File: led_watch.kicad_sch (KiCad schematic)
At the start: 107 parts, among them U3 M0G3507QDGS32RQ1, Y2 TXC-7C

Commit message: 4 layers, removed regulator
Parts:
- removed C1, C2: 10uF, Capacitor_SMD:C_0805_2012Metric_Pad1.18x1.45mm_HandSolder, symbol Device:C
- removed C3: 0.1uF, Capacitor_SMD:C_0805_2012Metric_Pad1.18x1.45mm_HandSolder, symbol Device:C
- removed L1: 2.2uH, Inductor_SMD:L_0805_2012Metric_Pad1.15x1.40mm_HandSolder, symbol Device:L
- removed PS1: TPS63031DSKR, Package_SON:WSON-10-1EP_2.5x2.5mm_P0.5mm_EP1.2x2mm_ThermalVias, symbol TPS63031DSKR:TPS63031DSKR
- renumbered R14 to R10, R6 to R11, R15 to R12, R7 to R13, R16 to R14, R8 to R15, R17 to R16, R9 to R17, R10 to R2, R2 to R3, R11 to R4, R3 to R5, R12 to R6, R4 to R7, R13 to R8, R5 to R9
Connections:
- net +3V3 is gone; now on net +VBATT: C7.1, C8.1, R19.1, U3.7 (VDD), Y2.1 (EN), Y2.4 (Vdd)
- net PA10: now also R10.2
- net PA11/SPI0_SCK: no longer R11.1
- net PA12: now also R15.1, R16.2; no longer R13.1
- net PA13/TFT_D/C: now also R13.1, R14.2; no longer R15.1
- net PA16/SPI1_POCI: no longer R4.1
- net PA17/SPI1_CLK: no longer R6.1
- net PA18/SPI1_PICO/BSL_Invoke: no longer R8.1
- net PA2: now also R4.2
- net PA21: no longer R18.1
- net PA22: no longer R16.1
- net PA23: no longer R14.1
- net PA24/TFT_RESET: no longer R12.1
- net PA25/SPI1_CS3: now also R11.1, R12.2; no longer R10.1
- net PA4: now also R2.2
- net PA5/HFXIN: now also R6.2
- net PA7: now also R18.2
- net PA8/SPI0_CS0: now also R8.2
- net PA9: no longer R2.1
- net at D1.2 (A), D2.2 (A), D3.2 (A)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: now also R2.1; no longer R2.2
- net at D33.2 (A), D34.2 (A), D35.2 (A)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: now also R10.1; no longer R10.2
- net at D17.2 (A), D18.2 (A), D19.2 (A)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: now also R6.1; no longer R6.2
- net at D57.2 (A), D58.2 (A), D59.2 (A)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: now also R16.1; no longer R16.2
- net at D10.2 (A), D11.2 (A), D12.2 (A)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: now also R4.1; no longer R4.2
- net at D41.2 (A), D42.2 (A), D43.2 (A)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: now also R12.1; no longer R12.2
- net at D25.2 (A), D26.2 (A), D27.2 (A)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: now also R8.1; no longer R8.2
- net at D65.2 (A), D66.2 (A), D67.2 (A)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: now also R18.1; no longer R18.2
- net at D49.2 (A), D50.2 (A), D51.2 (A)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: now also R14.1; no longer R14.2
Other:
- moved on the sheet: R10, R12, R14, R16, R18, R2, R4, R6, R8

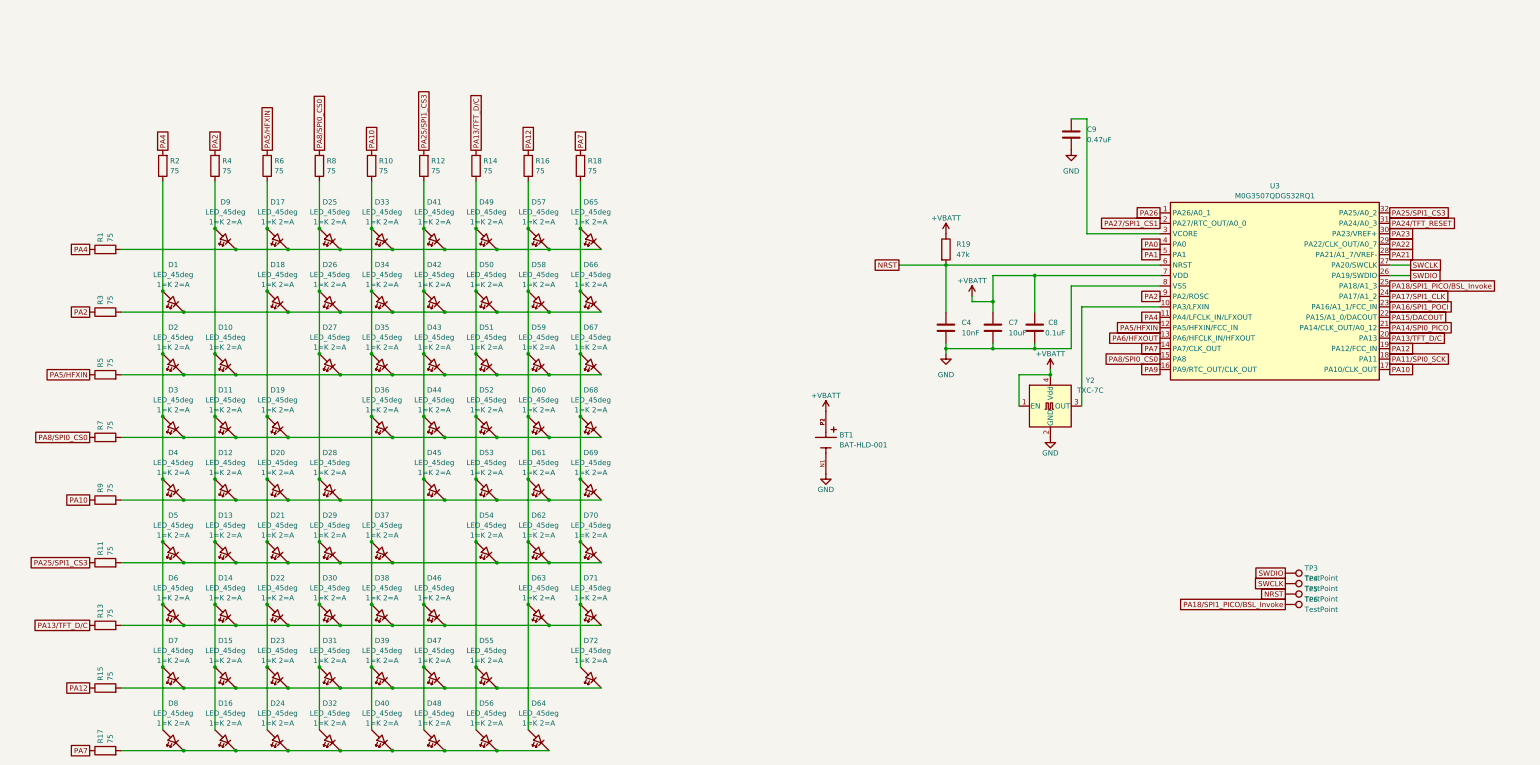
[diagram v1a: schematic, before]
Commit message: remove half of resistors, routing cleanup
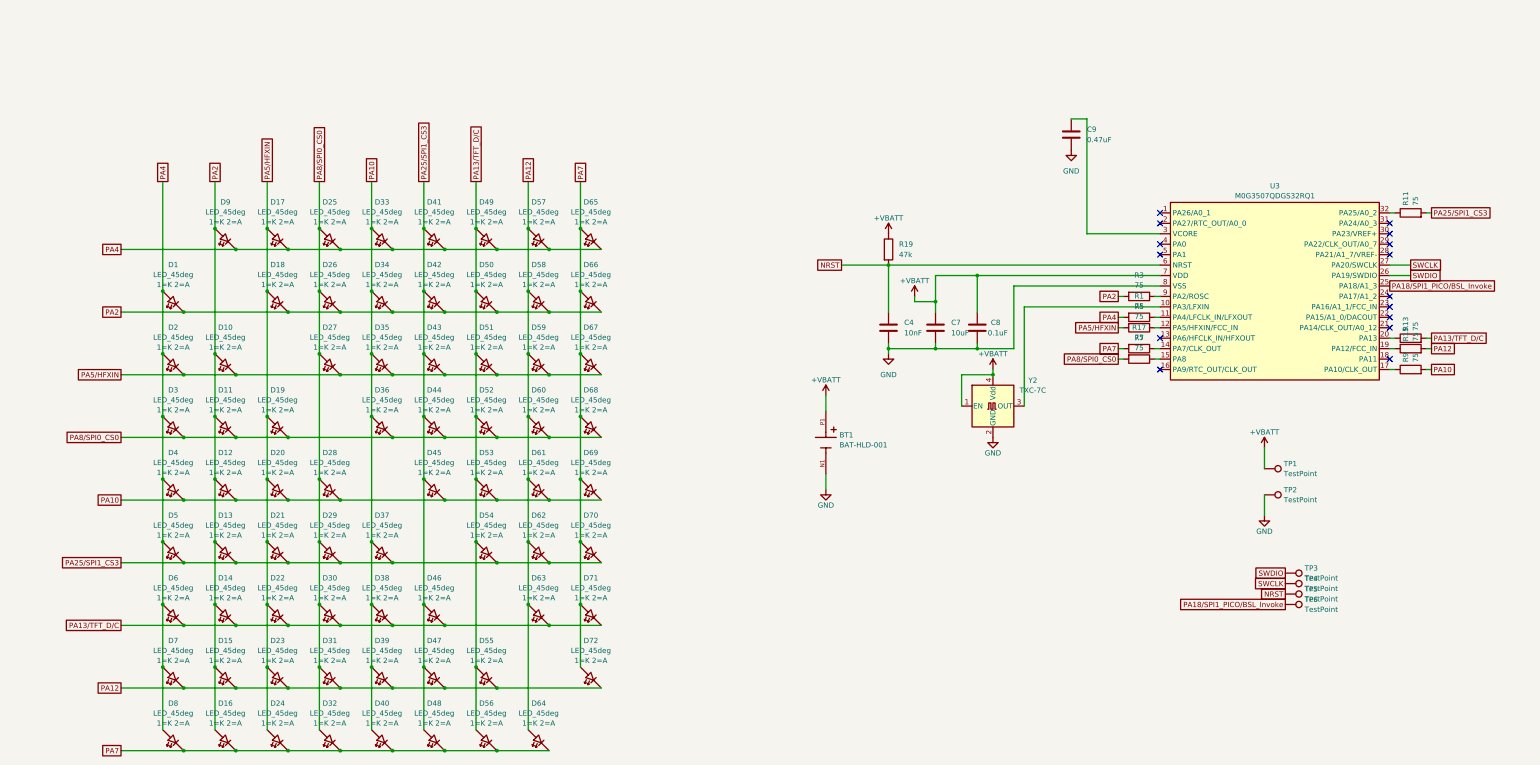
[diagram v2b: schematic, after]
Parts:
- removed R10, R12, R14, R16, R18, R2, R4, R6, R8: 75, Resistor_SMD:R_0805_2012Metric_Pad1.20x1.40mm_HandSolder, symbol Device:R
- added TP1, TP2: TestPoint, TestPoint:TestPoint_Pad_D1.0mm, symbol Connector:TestPoint
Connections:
- net +VBATT: now also TP1.1
- net GND: now also TP2.1
- net PA10: now also D12.1 (K), D20.1 (K), D28.1 (K), D33.2 (A), D34.2 (A), D35.2 (A), D36.2 (A), D37.2 (A), D38.2 (A), D39.2 (A), D4.1 (K), D40.2 (A), D45.1 (K), D53.1 (K), D61.1 (K), D69.1 (K), R9.2; no longer R9.1, U3.17 (PA10/CLK_OUT)
- net PA12: now also D15.1 (K), D23.1 (K), D31.1 (K), D39.1 (K), D47.1 (K), D55.1 (K), D57.2 (A), D58.2 (A), D59.2 (A), D60.2 (A), D61.2 (A), D62.2 (A), D63.2 (A), D64.2 (A), D7.1 (K), D72.1 (K), R15.2; no longer R15.1, U3.19 (PA12/FCC_IN)
- net PA13/TFT_D/C: now also D14.1 (K), D22.1 (K), D30.1 (K), D38.1 (K), D46.1 (K), D49.2 (A), D50.2 (A), D51.2 (A), D52.2 (A), D53.2 (A), D54.2 (A), D55.2 (A), D56.2 (A), D6.1 (K), D63.1 (K), D71.1 (K), R13.2; no longer R13.1, U3.20 (PA13)
- net PA2: now also D1.1 (K), D10.2 (A), D11.2 (A), D12.2 (A), D13.2 (A), D14.2 (A), D15.2 (A), D16.2 (A), D18.1 (K), D26.1 (K), D34.1 (K), D42.1 (K), D50.1 (K), D58.1 (K), D66.1 (K), D9.2 (A), R3.2; no longer R3.1, U3.9 (PA2/ROSC)
- net PA25/SPI1_CS3: now also D13.1 (K), D21.1 (K), D29.1 (K), D37.1 (K), D41.2 (A), D42.2 (A), D43.2 (A), D44.2 (A), D45.2 (A), D46.2 (A), D47.2 (A), D48.2 (A), D5.1 (K), D54.1 (K), D62.1 (K), D70.1 (K), R11.2; no longer R11.1, U3.32 (PA25/A0_2)
- net PA4: now also D1.2 (A), D17.1 (K), D2.2 (A), D25.1 (K), D3.2 (A), D33.1 (K), D4.2 (A), D41.1 (K), D49.1 (K), D5.2 (A), D57.1 (K), D6.2 (A), D65.1 (K), D7.2 (A), D8.2 (A), D9.1 (K), R1.2; no longer R1.1, U3.11 (PA4/LFCLK_IN/LFXOUT)
- net PA5/HFXIN: now also D10.1 (K), D17.2 (A), D18.2 (A), D19.2 (A), D2.1 (K), D20.2 (A), D21.2 (A), D22.2 (A), D23.2 (A), D24.2 (A), D27.1 (K), D35.1 (K), D43.1 (K), D51.1 (K), D59.1 (K), D67.1 (K), R5.2; no longer R5.1, U3.12 (PA5/HFXIN/FCC_IN)
- net PA7: now also D16.1 (K), D24.1 (K), D32.1 (K), D40.1 (K), D48.1 (K), D56.1 (K), D64.1 (K), D65.2 (A), D66.2 (A), D67.2 (A), D68.2 (A), D69.2 (A), D70.2 (A), D71.2 (A), D72.2 (A), D8.1 (K), R17.2; no longer R17.1, U3.14 (PA7/CLK_OUT)
- net PA8/SPI0_CS0: now also D11.1 (K), D19.1 (K), D25.2 (A), D26.2 (A), D27.2 (A), D28.2 (A), D29.2 (A), D3.1 (K), D30.2 (A), D31.2 (A), D32.2 (A), D36.1 (K), D44.1 (K), D52.1 (K), D60.1 (K), D68.1 (K), R7.2; no longer R7.1, U3.15 (PA8)
- net PA0: no longer names the net of U3.4 (PA0)
- net PA1: no longer names the net of U3.5 (PA1)
- net PA11/SPI0_SCK: no longer names the net of U3.18 (PA11)
- net PA14/SPI0_PICO: no longer names the net of U3.21 (PA14/CLK_OUT/A0_12)
- net PA15/DACOUT: no longer names the net of U3.22 (PA15/A1_0/DACOUT)
- net PA16/SPI1_POCI: no longer names the net of U3.23 (PA16/A1_1/FCC_IN)
- net PA17/SPI1_CLK: no longer names the net of U3.24 (PA17/A1_2)
- net PA21: no longer names the net of U3.28 (PA21/A1_7/VREF-)
- net PA22: no longer names the net of U3.29 (PA22/CLK_OUT/A0_7)
- net PA23: no longer names the net of U3.30 (PA23/VREF+)
- net PA24/TFT_RESET: no longer names the net of U3.31 (PA24/A0_3)
- net PA26: no longer names the net of U3.1 (PA26/A0_1)
- net PA27/SPI1_CS1: no longer names the net of U3.2 (PA27/RTC_OUT/A0_0)
- net PA6/HFXOUT: no longer names the net of U3.13 (PA6/HFCLK_IN/HFXOUT)
- net PA9: no longer names the net of U3.16 (PA9/RTC_OUT/CLK_OUT)
- new net: R11.1, U3.32 (PA25/A0_2)
- new net: R13.1, U3.20 (PA13)
- new net: R1.1, U3.11 (PA4/LFCLK_IN/LFXOUT)
- new net: R9.1, U3.17 (PA10/CLK_OUT)
- new net: R5.1, U3.12 (PA5/HFXIN/FCC_IN)
- new net: R17.1, U3.14 (PA7/CLK_OUT)
- new net: R7.1, U3.15 (PA8)
- new net: R15.1, U3.19 (PA12/FCC_IN)
- new net: R3.1, U3.9 (PA2/ROSC)
- no-connect marks 0 -> 15
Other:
- moved on the sheet: C4, C7, C8, R1, R11, R13, R15, R17, R19, R3, R5, R7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

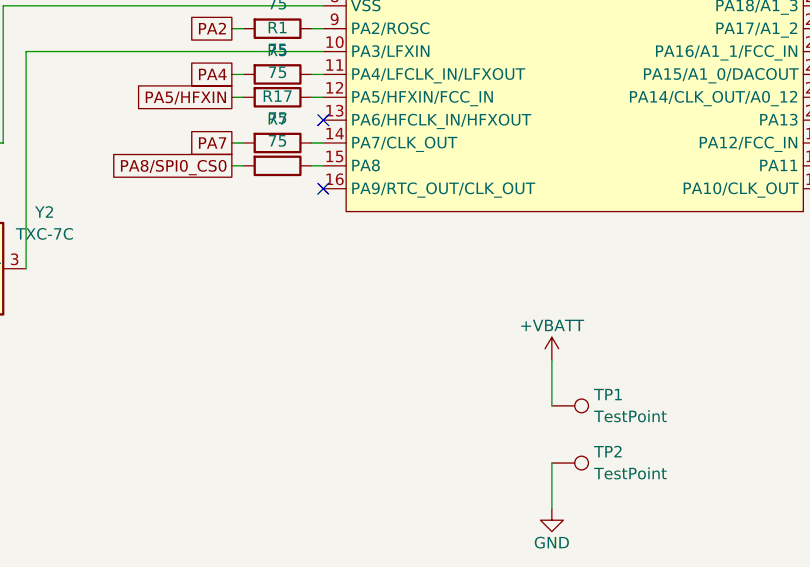
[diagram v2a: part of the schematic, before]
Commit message: add button
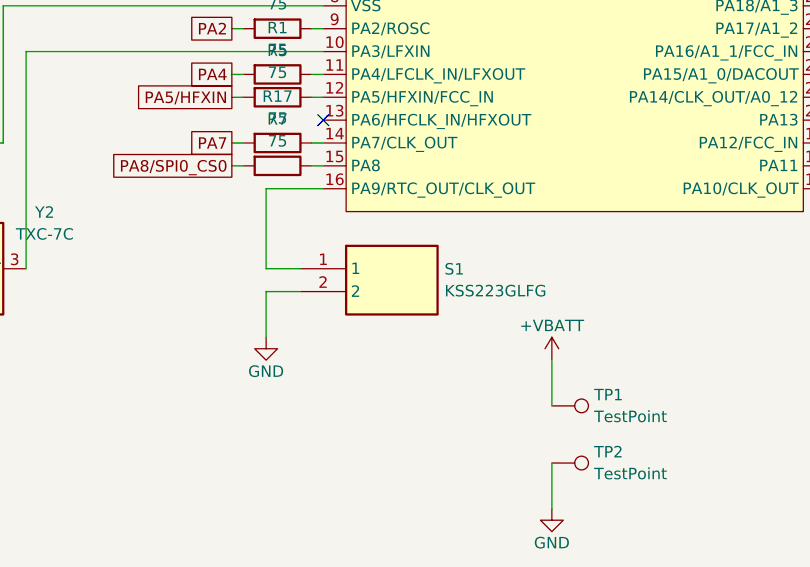
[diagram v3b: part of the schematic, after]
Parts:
- added S1: KSS223GLFG, KSS223GLFG, symbol KSS223GLFG:KSS223GLFG
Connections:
- net GND: now also S1.2
- net at U3.16 (PA9/RTC_OUT/CLK_OUT): now also S1.1
- no-connect marks 15 -> 14
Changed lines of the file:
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@@
 	)
 	(no_connect
-		(at 309.88 116.84)
-	)
-	(no_connect
 		(at 365.76 83.82)
 	)
@@
 	(wire
 		(pts
+			(xy 303.53 116.84) (xy 303.53 125.73)
+		)
+		(stroke
+			(width 0)
+			(type default)
+		)
+	)
+	(wire
+		(pts
 			(xy 308.61 104.14) (xy 309.88 104.14)
 		)
@@
 	(wire
 		(pts
+			(xy 303.53 125.73) (xy 307.34 125.73)
+		)
+		(stroke
+			(width 0)
+			(type default)
+		)
+	)
+	(wire
+		(pts
 			(xy 255.27 110.49) (xy 255.27 111.76)
 		)
@@
 	(wire
 		(pts
+			(xy 307.34 128.27) (xy 303.53 128.27)
+		)
+		(stroke
+			(width 0)
+			(type default)
+		)
+	)
+	(wire
+		(pts
 			(xy 67.31 189.23) (xy 67.31 204.47)
 		)
@@
 	(wire
 		(pts
+			(xy 303.53 128.27) (xy 303.53 133.35)
+		)
+		(stroke
+			(width 0)
+			(type default)
+		)
+	)
+	(wire
+		(pts
 			(xy 130.81 113.03) (xy 130.81 128.27)
 		)
@@
 	(wire
 		(pts
+			(xy 309.88 116.84) (xy 303.53 116.84)
+		)
+		(stroke
+			(width 0)
+			(type default)
+		)
+	)
+	(wire
+		(pts
 			(xy 276.86 101.6) (xy 276.86 125.73)
 		)
@@
 	)
 	(symbol
+		(lib_id "power:GND")
+		(at 303.53 133.35 0)
+		(unit 1)
+		(exclude_from_sim no)
+		(in_bom yes)
+		(on_board yes)
+		(dnp no)
+		(property "Reference" "#PWR05"
+			(at 303.53 139.7 0)
+			(effects
+				(font
+					(size 1.27 1.27)
+				)
+				(hide yes)
+			)
+		)
+		(property "Value" "GND"
+			(at 303.53 137.16 0)
+			(effects
+				(font
+					(size 1.27 1.27)
+				)
+			)
+		)
+		(property "Footprint" ""
+			(at 303.53 133.35 0)
+			(effects
+				(font
+					(size 1.27 1.27)
+				)
+				(hide yes)
+			)
+		)
+		(property "Datasheet" ""
+			(at 303.53 133.35 0)
+			(effects
+				(font
+					(size 1.27 1.27)
+				)
+				(hide yes)
+			)
+		)
+		(property "Description" "Power symbol creates a global label with name \"GND\" , ground"
+			(at 303.53 133.35 0)
+			(effects
+				(font
+					(size 1.27 1.27)
+				)
+				(hide yes)
+			)
+		)
+		(pin "1"
+		)
+		(instances
+			(project "led_watch"
+				(path "/2ba2d868-0c1e-438d-873d-80061e515404"
+					(reference "#PWR05")
+					(unit 1)
+				)
+			)
+		)
+	)
+	(symbol
 		(lib_id "Device:LED_45deg")
 		(at 107.95 191.77 0)
@@
 					(unit 1)
 				)
+			)
+		)
+	)
+	(symbol
+		(lib_id "KSS223GLFG:KSS223GLFG")
+		(at 307.34 125.73 0)
+		(unit 1)
+		(exclude_from_sim no)
+		(in_bom yes)
+		(on_board yes)
+		(dnp no)
+		(fields_autoplaced yes)
+		(property "Reference" "S1"
+			(at 323.342 125.7878 0)
+			(effects
+				(font
+					(size 1.27 1.27)
+				)
+				(justify left)
+			)
+		)
+		(property "Value" "KSS223GLFG"
+			(at 323.342 128.2121 0)
+			(effects
+				(font
+					(size 1.27 1.27)
+				)
+				(justify left)
+			)
+		)
+		(property "Footprint" "KSS223GLFG"
+			(at 323.85 220.65 0)
+			(effects
+				(font
+					(size 1.27 1.27)
+				)
+				(justify left top)
+				(hide yes)
+			)
+		)
+		(property "Datasheet" ""
+			(at 323.85 320.65 0)
+			(effects
+				(font
+					(size 1.27 1.27)
+				)
+				(justify left top)
+				(hide yes)
+			)
+		)
+		(property "Description" "Tactile Switches Gold 200Gf Gullwing"
+			(at 307.34 125.73 0)
+			(effects
+				(font
+					(size 1.27 1.27)
+				)
+				(hide yes)
+			)
+		)
+		(property "Height" "1.7"
+			(at 323.85 520.65 0)
+			(effects
+				(font
+					(size 1.27 1.27)
+				)
+				(justify left top)
+				(hide yes)
+			)
+		)
+		(property "Mouser Part Number" "611-KSS223GLFG"
+			(at 323.85 620.65 0)
+			(effects
+				(font
+					(size 1.27 1.27)
+				)
+				(justify left top)
+				(hide yes)
+			)
+		)
+		(property "Mouser Price/Stock" "https://www.mouser.co.uk/ProductDetail/CK/KSS223GLFG/?qs=vOd3edNlRKDrjmqWpM8YJA%3D%3D"
+			(at 323.85 720.65 0)
+			(effects
+				(font
+					(size 1.27 1.27)
+				)
+				(justify left top)
+				(hide yes)
+			)
+		)
+		(property "Manufacturer_Name" "C & K COMPONENTS"
+			(at 323.85 820.65 0)
+			(effects
+				(font
+					(size 1.27 1.27)
+				)
+				(justify left top)
+				(hide yes)
+			)
+		)
+		(property "Manufacturer_Part_Number" "KSS223GLFG"
+			(at 323.85 920.65 0)
+			(effects
+				(font
+					(size 1.27 1.27)
+				)
+				(justify left top)
+				(hide yes)
+			)
+		)
+		(pin "2"
+		)
+		(pin "1"
+		)
+		(instances
+			(project ""
+				(path "/2ba2d868-0c1e-438d-873d-80061e515404"
+					(reference "S1")
+					(unit 1)
+				)
